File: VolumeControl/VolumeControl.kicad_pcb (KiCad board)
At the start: 2 copper layers, 5 parts, among them U2 MCP4251-xxxx-SL

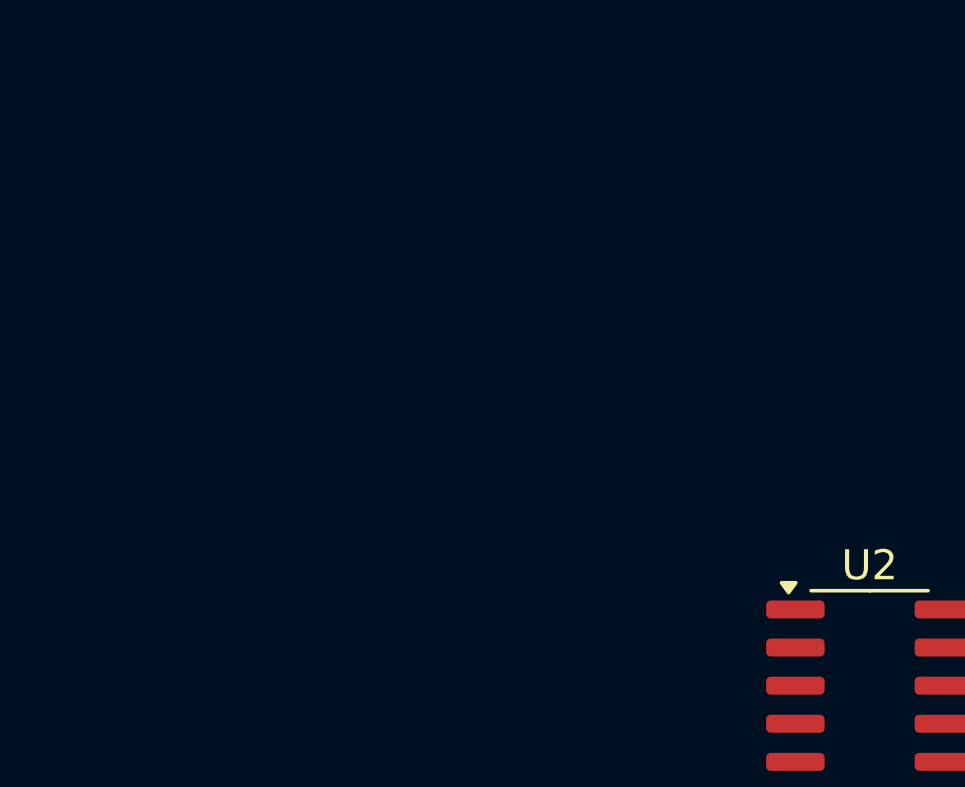
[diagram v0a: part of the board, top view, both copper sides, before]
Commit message: 6 Opamps
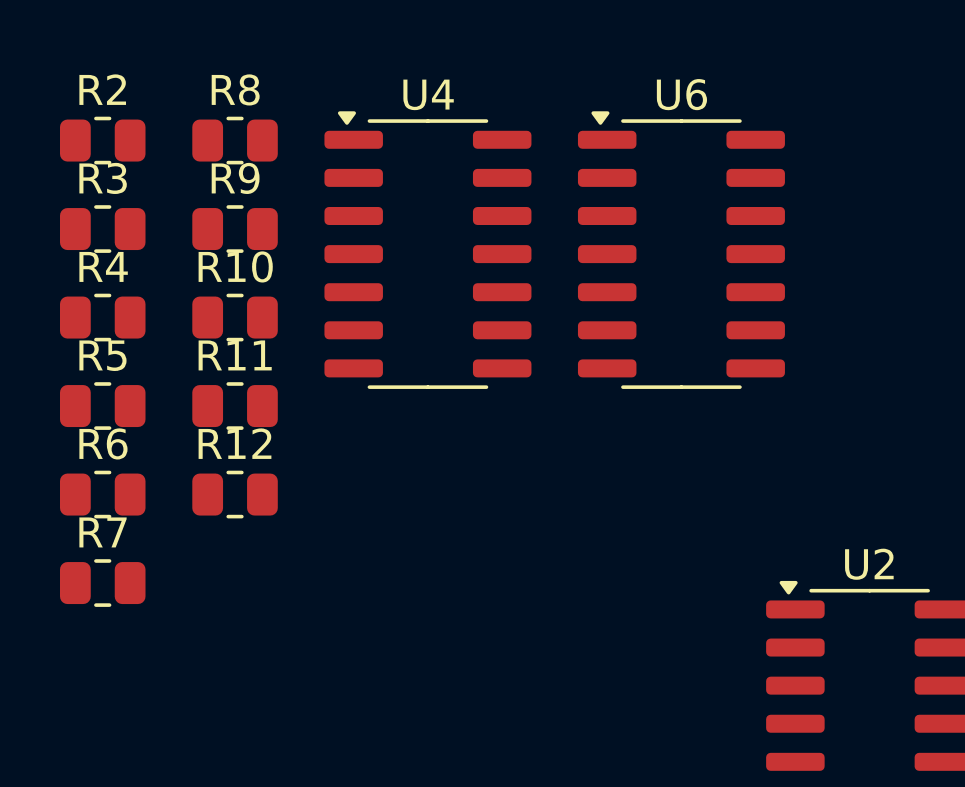
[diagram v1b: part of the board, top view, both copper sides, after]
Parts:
- added R10: 100k, Resistor_SMD:R_0805_2012Metric, F.Cu at (48.8, 44.1)
- added R11: 100k, Resistor_SMD:R_0805_2012Metric, F.Cu at (48.8, 47.1)
- added R12: 100k, Resistor_SMD:R_0805_2012Metric, F.Cu at (48.8, 50.0)
- added R2: 100k, Resistor_SMD:R_0805_2012Metric, F.Cu at (44.4, 38.2)
- added R3: 100k, Resistor_SMD:R_0805_2012Metric, F.Cu at (44.4, 41.2)
- added R4: 100k, Resistor_SMD:R_0805_2012Metric, F.Cu at (44.4, 44.1)
- added R5: 100k, Resistor_SMD:R_0805_2012Metric, F.Cu at (44.4, 47.1)
- added R6: 100k, Resistor_SMD:R_0805_2012Metric, F.Cu at (44.4, 50.0)
- added R7: 100k, Resistor_SMD:R_0805_2012Metric, F.Cu at (44.4, 53.0)
- added R8: 100k, Resistor_SMD:R_0805_2012Metric, F.Cu at (48.8, 38.2)
- added R9: 100k, Resistor_SMD:R_0805_2012Metric, F.Cu at (48.8, 41.2)
- added U4: MCP4251-xxxx-SL, Package_SO:SOIC-14_3.9x8.7mm_P1.27mm, F.Cu at (55.3, 42.0)
- added U6: MCP4251-xxxx-SL, Package_SO:SOIC-14_3.9x8.7mm_P1.27mm, F.Cu at (63.7, 42.0)
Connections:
- C1 pad 1: unconnected-(C1-Pad1) -> VCC
- C1 pad 2: unconnected-(C1-Pad2) -> GND
- D2 pad 1: unconnected-(D2-K-Pad1) -> Net-(D2-K)
- D2 pad 2: unconnected-(D2-A-Pad2) -> Net-(D2-A)
- R1 pad 1: unconnected-(R1-Pad1) -> Net-(J3-Pin_2)
- R1 pad 2: unconnected-(R1-Pad2) -> GND
- U2 pad 14: unconnected-(U2-VDD-Pad14) -> VCC
- U2 pad 4: unconnected-(U2-VSS-Pad4) -> GND
- U2 pad 7: unconnected-(U2-P1A-Pad7) -> Net-(U2-P1A)
- U2 pad 8: unconnected-(U2-P0A-Pad8) -> Net-(U2-P0A)

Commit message: circuito quase completo
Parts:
- removed D1: 1N4001, Diode_THT:D_DO-41_SOD81_P10.16mm_Horizontal
- added C10: 10u, Capacitor_SMD:C_1210_3225Metric_Pad1.33x2.70mm_HandSolder, F.Cu at (49.5, 120.7)
- added C11: 10u, Capacitor_SMD:C_1210_3225Metric_Pad1.33x2.70mm_HandSolder, F.Cu at (56.5, 137.7)
- added C12: 50p, Capacitor_SMD:C_0805_2012Metric_Pad1.18x1.45mm_HandSolder, F.Cu at (34.5, 131.7)
- added C13: 50p, Capacitor_SMD:C_0805_2012Metric_Pad1.18x1.45mm_HandSolder, F.Cu at (41.5, 141.7)
- added C14: 10u, Capacitor_SMD:C_1210_3225Metric_Pad1.33x2.70mm_HandSolder, F.Cu at (35.5, 127.7)
- added C15: 10u, Capacitor_SMD:C_1210_3225Metric_Pad1.33x2.70mm_HandSolder, F.Cu at (42.5, 137.7)
- added C16: 10u, Capacitor_SMD:C_1210_3225Metric_Pad1.33x2.70mm_HandSolder, F.Cu at (42.5, 127.7)
- added C17: 10u, Capacitor_SMD:C_1210_3225Metric_Pad1.33x2.70mm_HandSolder, F.Cu at (42.5, 122.7)
- added C18: 50p, Capacitor_SMD:C_0805_2012Metric_Pad1.18x1.45mm_HandSolder, F.Cu at (46.5, 141.7)
- added C19: 50p, Capacitor_SMD:C_0805_2012Metric_Pad1.18x1.45mm_HandSolder, F.Cu at (50.5, 101.7)
- added C2: 100uF, Capacitor_SMD:CP_Elec_5x3.9, F.Cu at (52.5, 112.7)
- added C20: 10u, Capacitor_SMD:C_1210_3225Metric_Pad1.33x2.70mm_HandSolder, F.Cu at (49.5, 137.7)
- added C21: 10u, Capacitor_SMD:C_1210_3225Metric_Pad1.33x2.70mm_HandSolder, F.Cu at (56.5, 101.7)
- added C22: 50p, Capacitor_SMD:C_0805_2012Metric_Pad1.18x1.45mm_HandSolder, F.Cu at (47.5, 107.7)
- added C23: 50p, Capacitor_SMD:C_0805_2012Metric_Pad1.18x1.45mm_HandSolder, F.Cu at (42.5, 109.7)
- added C24: 100nF, Capacitor_SMD:C_0805_2012Metric, F.Cu at (43.5, 118.7)
- added C25: 100nF, Capacitor_SMD:C_0805_2012Metric, F.Cu at (45.5, 115.7)
- added C26: 100nF, Capacitor_SMD:C_0805_2012Metric, F.Cu at (40.5, 115.7)
- added C27: 100nF, Capacitor_SMD:C_0805_2012Metric, F.Cu at (40.5, 112.7)
- added C28: 100nF, Capacitor_SMD:C_0805_2012Metric, F.Cu at (63.5, 88.7)
- added C29: 100uF, Capacitor_SMD:CP_Elec_5x3.9, F.Cu at (70.5, 94.7)
- added C3: 100uF, Capacitor_SMD:CP_Elec_5x3.9, F.Cu at (70.5, 101.7)
- added C4: 10u, Capacitor_SMD:C_1210_3225Metric_Pad1.33x2.70mm_HandSolder, F.Cu at (56.5, 96.7)
- added C5: 50p, Capacitor_SMD:C_0805_2012Metric_Pad1.18x1.45mm_HandSolder, F.Cu at (50.5, 97.7)
- added C6: 50p, Capacitor_SMD:C_0805_2012Metric_Pad1.18x1.45mm_HandSolder, F.Cu at (42.5, 106.7)
- added C7: 10u, Capacitor_SMD:C_1210_3225Metric_Pad1.33x2.70mm_HandSolder, F.Cu at (53.5, 106.7)
- added C8: 10u, Capacitor_SMD:C_1210_3225Metric_Pad1.33x2.70mm_HandSolder, F.Cu at (80.5, 95.7)
- added C9: 10u, Capacitor_SMD:C_1210_3225Metric_Pad1.33x2.70mm_HandSolder, F.Cu at (96.5, 98.5)
- added J1: Barrel_Jack, Connector_BarrelJack:BarrelJack_CUI_PJ-063AH_Horizontal, F.Cu at (115.5, 77.0)
- added J10: Conn_01x03, Connector_PinHeader_1.00mm:PinHeader_1x03_P1.00mm_Vertical, F.Cu at (41.5, 131.7)
- added J11: Conn_01x03, Connector_PinHeader_1.00mm:PinHeader_1x03_P1.00mm_Vertical, F.Cu at (38.5, 131.7)
- added J12: Conn_01x03, Connector_PinHeader_1.00mm:PinHeader_1x03_P1.00mm_Vertical, F.Cu at (53.5, 131.7)
- added J13: Conn_01x03, Connector_PinHeader_1.00mm:PinHeader_1x03_P1.00mm_Vertical, F.Cu at (61.5, 102.7)
- added J2: Conn_01x03, Connector_PinHeader_1.00mm:PinHeader_1x03_P1.00mm_Vertical, F.Cu at (64.5, 102.7)
- added J3: Conn_01x03, Connector_PinHeader_1.00mm:PinHeader_1x03_P1.00mm_Vertical, F.Cu at (61.5, 97.7)
- added J4: Conn_01x03, Connector_PinHeader_1.00mm:PinHeader_1x03_P1.00mm_Vertical, F.Cu at (50.5, 131.7)
- added J5: Conn_01x03, Connector_PinHeader_1.00mm:PinHeader_1x03_P1.00mm_Vertical, F.Cu at (64.5, 97.7)
- added J6: Conn_01x03, Connector_PinHeader_1.00mm:PinHeader_1x03_P1.00mm_Vertical, F.Cu at (47.5, 126.7)
- added J7: Conn_01x03, Connector_PinHeader_1.00mm:PinHeader_1x03_P1.00mm_Vertical, F.Cu at (56.5, 131.7)
- added J8: Conn_01x03, Connector_PinHeader_1.00mm:PinHeader_1x03_P1.00mm_Vertical, F.Cu at (44.5, 131.7)
- added J9: Conn_01x03, Connector_PinHeader_1.00mm:PinHeader_1x03_P1.00mm_Vertical, F.Cu at (47.5, 131.7)
- added R13: 100k, Resistor_SMD:R_0805_2012Metric, F.Cu at (47.5, 104.7)
- added R14: 100k, Resistor_SMD:R_0805_2012Metric, F.Cu at (42.5, 103.7)
- added R15: 100k, Resistor_SMD:R_0805_2012Metric, F.Cu at (58.5, 92.7)
- added U1: OPA1612AxD, Package_SO:SOIC-8-1EP_3.9x4.9mm_P1.27mm_EP2.29x3mm, F.Cu at (79.5, 101.7)
- added U10: LM1117MP-5.0, Package_TO_SOT_SMD:SOT-223-3_TabPin2, F.Cu at (70.5, 109.7)
- added U3: L7812, Package_TO_SOT_SMD:TO-252-3_TabPin2, F.Cu at (131.6, 75.7)
- added U5: OPA1612AxD, Package_SO:SOIC-8-1EP_3.9x4.9mm_P1.27mm_EP2.29x3mm, F.Cu at (55.5, 126.7)
- added U7: OPA1612AxD, Package_SO:SOIC-8-1EP_3.9x4.9mm_P1.27mm_EP2.29x3mm, F.Cu at (57.5, 119.7)
- added U8: OPA1612AxD, Package_SO:SOIC-8-1EP_3.9x4.9mm_P1.27mm_EP2.29x3mm, F.Cu at (61.5, 110.7)
- added U9: WEMOS_D1_mini, RF_Module:WEMOS_D1_mini_light, F.Cu at (63.5, 133.7)
- C1: footprint Capacitor_SMD:C_0805_2012Metric -> Capacitor_SMD:C_0805_2012Metric_Pad1.18x1.45mm_HandSolder
- moved C1 566.3 mm to (45.5, 112.7)
- moved R1 549.2 mm to (63.5, 94.7)
- moved D2 486.1 mm to (122.0, 76.5), turned to 180 degrees
- moved R2 106.6 mm to (49.5, 144.7)
- moved R8 106.6 mm to (44.5, 144.7)
- moved R11 97.8 mm to (54.5, 144.7)
- moved R9 94.8 mm to (33.5, 134.7)
- moved R6 92.3 mm to (55.5, 141.7)
- moved R10 89.7 mm to (29.5, 131.7)
- moved U4 80.3 mm to (75.5, 119.7)
- moved U6 77.7 mm to (66.5, 119.7)
- moved R5 74.0 mm to (36.5, 120.7)
- moved R7 71.2 mm to (36.5, 123.7)
- moved U2 63.7 mm to (84.5, 119.7)
- moved R3 60.9 mm to (78.5, 91.7)
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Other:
- board outline added: 116.5 x 76.5 mm
- board text added: "0.0000 mm / 0.0000 mm"
- board text added: "0.3000 mm"
- board text added: "1.6000 mm"
- board text added: "2"
- board text added: "81.5808 mm x 89.8315 mm"
- board text added: "BOARD CHARACTERISTICS"
- board text added: "Board Thickness:"
- board text added: "Board overall dimensions:"
- board text added: "Castellated pads:"
- board text added: "Copper Finish:"
- board text added: "Copper Layer Count:"
- board text added: "Edge card connectors:"
- board text added: "Impedance Control:"
- board text added: "Min hole diameter:"
- board text added: "Min track/spacing:"
- board text added: "No"
- board text added: "None"
- board text added: "Plated Board Edge:"

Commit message: layout upates
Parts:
- added D1: LED, LED_SMD:LED_1210_3225Metric, F.Cu at (150.5, 78.6)
- added R16: 560R, Resistor_SMD:R_0805_2012Metric, F.Cu at (150.5, 74.0)
- moved C28 113.5 mm to (176.5, 78.5), turned to 90 degrees
- moved J4 112.5 mm to (160.5, 108.0)
- moved R2 110.7 mm to (153.9, 108.0)
- moved C6 102.8 mm to (145.0, 114.5), turned to 90 degrees
- moved C29 102.7 mm to (171.5, 76.2), turned to 90 degrees
- moved J3 99.0 mm to (160.5, 98.0)
- moved C2 99.0 mm to (144.0, 75.0), turned to 90 degrees
- moved C1 96.4 mm to (138.0, 85.5), turned to 180 degrees
- moved U10 96.2 mm to (161.0, 77.0)
- moved C5 95.2 mm to (145.5, 104.0), turned to 90 degrees
- moved C7 93.5 mm to (146.9, 109.5)
- moved R1 90.6 mm to (154.0, 98.5)
- moved C4 90.0 mm to (146.4, 98.5)
- moved C3 64.8 mm to (129.5, 75.0), turned to 90 degrees
- moved R4 59.0 mm to (119.6, 110.0)
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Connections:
- U2 pad 14: VCC -> V5V
- U4 pad 14: VCC -> V5V
- U6 pad 14: VCC -> V5V
- U9 pad 14: unconnected-(U9-SCL/D1-Pad14) -> SCL
- U9 pad 4: unconnected-(U9-SCK/D5-Pad4) -> SCK
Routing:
- net GND: track 0.00 -> 91.6 mm
- net VCC: track 0.00 -> 23.7 mm
- net Net-(D2-K): track 0.00 -> 13.9 mm
- net V5V: track 0.00 -> 13.3 mm
- net Net-(D2-A): track 0.00 -> 4.71 mm
- net Net-(D1-K): track 0.00 -> 2.29 mm
- added copper zone on F.Cu, net GND
- added copper zone on F.Cu, net V5V
- added copper zone on F.Cu, net VCC

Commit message: improvements on PCB design - PCB placement finished -missing controller
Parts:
- added FB1: FerriteBead_Small, Resistor_SMD:R_1206_3216Metric_Pad1.30x1.75mm_HandSolder, F.Cu at (112.0, 78.0)
- added R17: 10R, Resistor_SMD:R_0805_2012Metric, F.Cu at (115.5, 78.1)
- U1, U5, U7, U8: footprint Package_SO:SOIC-8-1EP_3.9x4.9mm_P1.27mm_EP2.29x3mm -> Package_SO:SOIC-8_3.9x4.9mm_P1.27mm
- moved R7 142.4 mm to (178.5, 113.6), turned to 90 degrees
- moved C22 139.3 mm to (182.5, 73.6), turned to 180 degrees
- moved J8 138.6 mm to (182.0, 114.1)
- moved C12 137.6 mm to (170.6, 111.1), turned to 180 degrees
- moved C14 136.1 mm to (171.0, 114.1)
- moved R8 135.2 mm to (178.5, 126.6), turned to 90 degrees
- moved J9 134.6 mm to (182.0, 126.6)
- moved R13 134.4 mm to (178.5, 74.6), turned to 90 degrees
- moved R12 133.2 mm to (178.5, 147.6), turned to 90 degrees
- moved C23 133.2 mm to (173.5, 85.6), turned to 180 degrees
- moved R14 132.8 mm to (172.1, 74.6)
- moved C27 132.0 mm to (168.0, 78.6), turned to -90 degrees
- moved C13 130.7 mm to (171.0, 124.1), turned to 180 degrees
- moved C15 129.0 mm to (171.1, 127.6)
- moved J12 128.7 mm to (182.0, 138.1)
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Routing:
- net GND: track 91.6 -> 203.7 mm, vias 0 -> 3
- net Earth: track 0.00 -> 44.5 mm
- net Net-(U1B--): track 0.00 -> 39.7 mm
- net Net-(U1A-+): track 0.00 -> 29.5 mm, vias 0 -> 2
- net Net-(U1A--): track 0.00 -> 21.7 mm
- net VCC: track 23.7 -> 45.3 mm
- net Net-(U2-P0A): track 0.00 -> 17.5 mm
- net Net-(U2-P1A): track 0.00 -> 17.1 mm
- net Net-(R15-Pad1): track 0.00 -> 12.1 mm
- net Net-(U1B-+): track 0.00 -> 12.0 mm
- net Net-(U8A-+): track 0.00 -> 10.5 mm
- net Net-(J3-Pin_2): track 0.00 -> 9.71 mm
- net Net-(J4-Pin_2): track 0.00 -> 9.57 mm
- net Net-(J2-Pin_2): track 0.00 -> 9.19 mm
- net Net-(J5-Pin_2): track 0.00 -> 9.15 mm
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- added copper zone on F.Cu, net Earth
- added copper zone on B.Cu, net GND
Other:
- board size 116.5 x 76.5 mm -> 76.5 x 94.5 mm

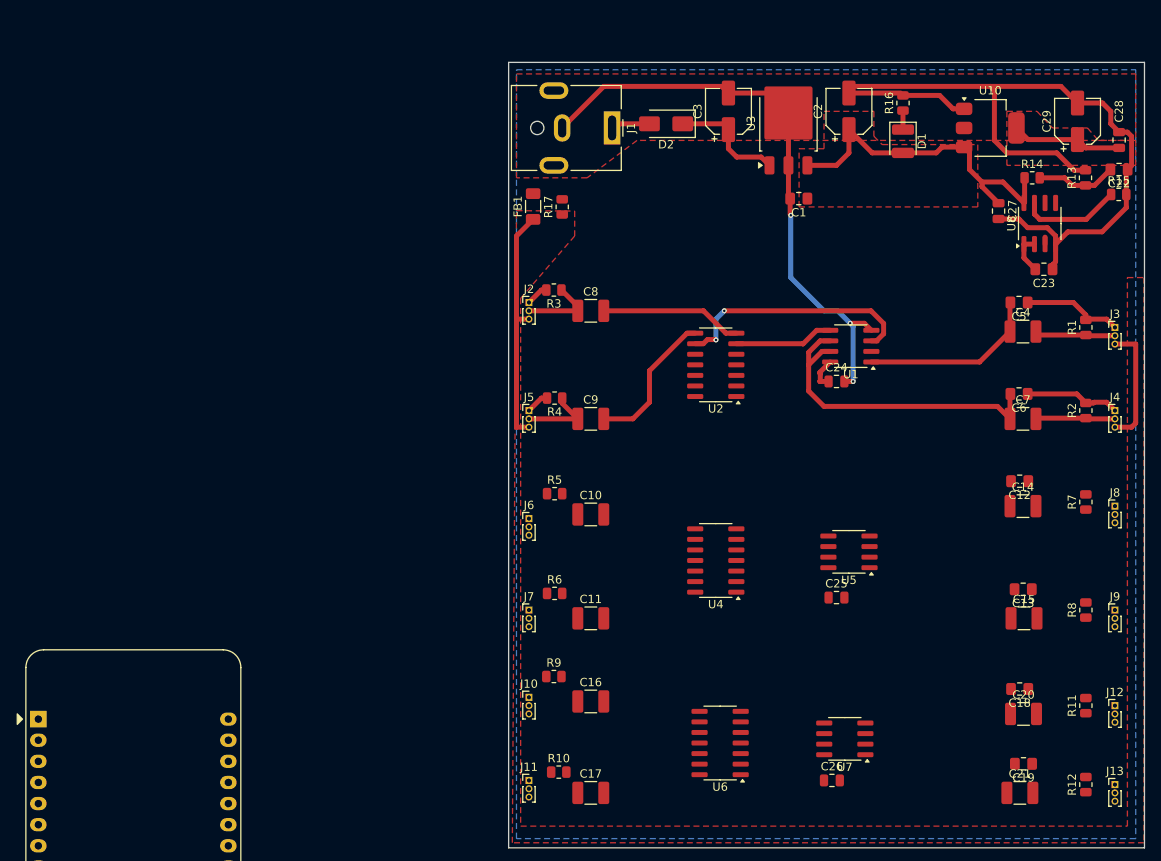
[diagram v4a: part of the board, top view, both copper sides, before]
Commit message: simulation update, schematic update for only one input
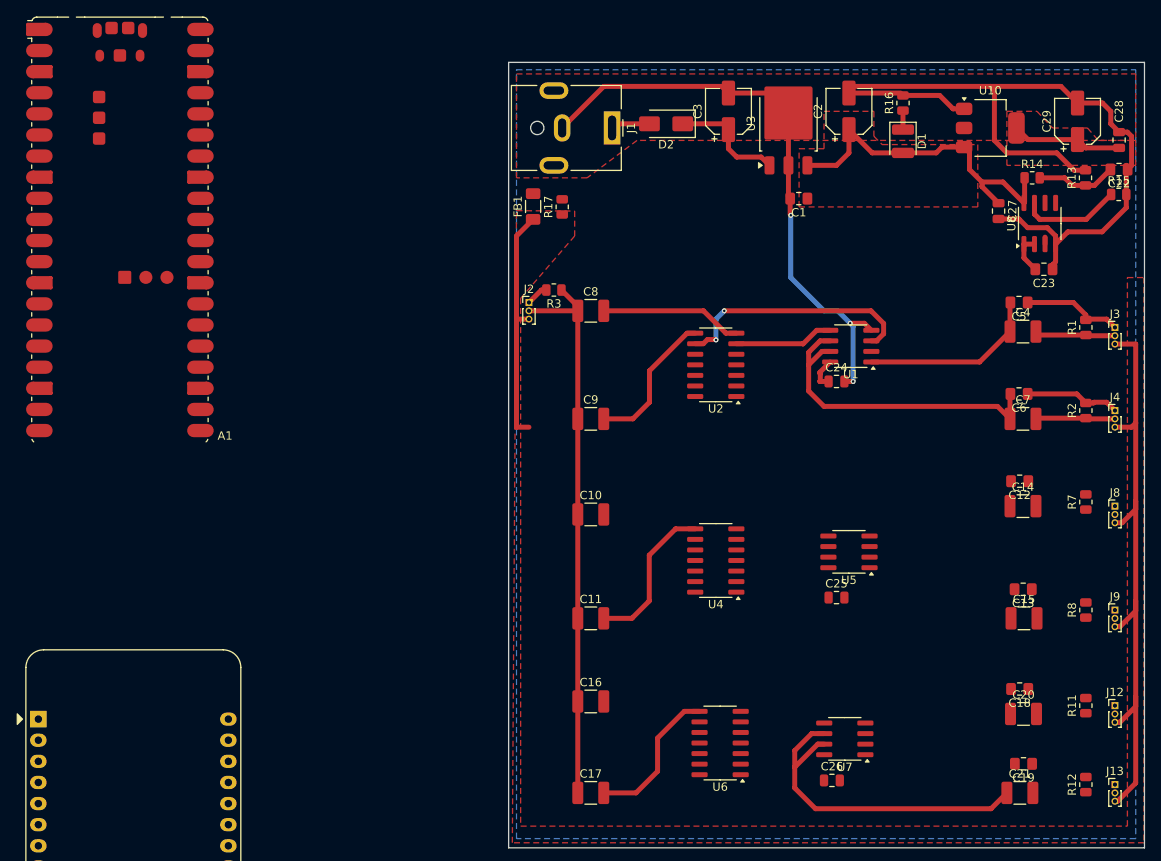
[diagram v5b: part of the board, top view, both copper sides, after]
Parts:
- removed J10, J11, J5, J6, J7: Conn_01x03, Connector_PinHeader_1.00mm:PinHeader_1x03_P1.00mm_Vertical
- removed R10, R4, R5, R6, R9: 100k, Resistor_SMD:R_0805_2012Metric
- added A1: RaspberryPi_Pico_W, Module:RaspberryPi_Pico_W_SMD, F.Cu at (62.3, 80.9)
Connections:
- C10 pad 1: Net-(J6-Pin_2) -> Net-(J2-Pin_2)
- C10 pad 2: Net-(U4-P1A) -> Net-(U2-P1A)
- C11 pad 1: Net-(J7-Pin_2) -> Net-(J2-Pin_2)
- C16 pad 1: Net-(J10-Pin_2) -> Net-(J2-Pin_2)
- C17 pad 1: Net-(J11-Pin_2) -> Net-(J2-Pin_2)
- C9 pad 1: Net-(J5-Pin_2) -> Net-(J2-Pin_2)
- U2 pad 13: unconnected-(U2-SDO-Pad13) -> Net-(U2-P1A)
- U4 pad 7: Net-(U4-P1A) -> Net-(U2-P1A)
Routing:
- net Earth: track 44.5 -> 104.4 mm
- net Net-(J2-Pin_2): track 9.19 -> 67.2 mm
- net Net-(U7B--): track 0.00 -> 40.9 mm
- net Net-(U4-P0A): track 0.00 -> 18.7 mm
- net Net-(U6-P0A): track 0.00 -> 17.9 mm
- net Net-(J5-Pin_2): track 9.15 -> 0.00 mm
- net GND: track 203.7 -> 200.9 mm

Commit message: PPT first draft
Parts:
- removed A1: RaspberryPi_Pico_W, Module:RaspberryPi_Pico_W_SMD
- removed U9: WEMOS_D1_mini, RF_Module:WEMOS_D1_mini_light
- added D3: LED, LED_SMD:LED_1210_3225Metric, F.Cu at (312.4, 117.3)
- added D4: LED, LED_SMD:LED_1210_3225Metric, F.Cu at (312.4, 121.6)
- added D5: LED, LED_SMD:LED_1210_3225Metric, F.Cu at (312.4, 125.8)
- added D6: LED, LED_SMD:LED_1210_3225Metric, F.Cu at (312.4, 130.1)
- added D7: LED, LED_SMD:LED_1210_3225Metric, F.Cu at (312.4, 134.4)
- added D8: LED, LED_SMD:LED_1210_3225Metric, F.Cu at (312.4, 138.7)
- added R10: 100R, Resistor_SMD:R_0805_2012Metric, F.Cu at (330.2, 119.5)
- added R18: 100R, Resistor_SMD:R_0805_2012Metric, F.Cu at (330.2, 122.5)
- added R19: 10K, Resistor_SMD:R_0805_2012Metric, F.Cu at (334.6, 116.6)
- added R20: 10K, Resistor_SMD:R_0805_2012Metric, F.Cu at (334.6, 119.5)
- added R21: 10K, Resistor_SMD:R_0805_2012Metric, F.Cu at (334.6, 122.5)
- added R4: 100R, Resistor_SMD:R_0805_2012Metric, F.Cu at (325.8, 116.6)
- added R5: 100R, Resistor_SMD:R_0805_2012Metric, F.Cu at (325.8, 119.5)
- added R6: 100R, Resistor_SMD:R_0805_2012Metric, F.Cu at (325.8, 122.5)
- added R9: 100R, Resistor_SMD:R_0805_2012Metric, F.Cu at (330.2, 116.6)
- added SW1: Select, Button_Switch_SMD:SW_SPST_PTS647_Sx50, F.Cu at (319.4, 118.3)
- added SW2: Up, Button_Switch_SMD:SW_SPST_PTS647_Sx50, F.Cu at (319.4, 124.8)
- added SW3: Down, Button_Switch_SMD:SW_SPST_PTS647_Sx50, F.Cu at (319.4, 131.2)
- added U12: ESP32-S3-DevKitC, Espressif:ESP32-S3-DevKitC, F.Cu at (189.7, 148.0)
- moved C23 81.2 mm to (246.0, 49.1)
- moved R13 81.2 mm to (251.0, 38.1)
- moved R14 81.2 mm to (244.5, 38.1)
- moved R15 81.2 mm to (255.0, 40.1)
- moved U2 81.2 mm to (206.5, 60.6)
- moved U4 81.2 mm to (206.5, 84.1)
- moved U8 81.2 mm to (245.5, 43.6)
- moved C12 81.2 mm to (243.0, 74.6)
- moved C18 81.2 mm to (243.0, 99.6)
- moved C26 81.2 mm to (220.5, 110.6)
- moved C1 81.2 mm to (216.5, 40.6)
- moved C10 81.2 mm to (191.4, 78.6)
- moved C11 81.2 mm to (191.4, 91.1)
- moved C13 81.2 mm to (243.5, 87.6)
- moved C14 81.2 mm to (243.4, 77.6)
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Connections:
- C10 pad 2: Net-(U2-P1A) -> Net-(U4-P1A)
- U2 pad 1: unconnected-(U2-~{CS}-Pad1) -> CS0
- U2 pad 13: Net-(U2-P1A) -> MISO
- U2 pad 2: unconnected-(U2-SCK-Pad2) -> SCK
- U2 pad 3: unconnected-(U2-SDI-Pad3) -> MOSI
- U4 pad 1: unconnected-(U4-~{CS}-Pad1) -> CS1
- U4 pad 13: unconnected-(U4-SDO-Pad13) -> MISO
- U4 pad 2: unconnected-(U4-SCK-Pad2) -> SCK
- U4 pad 3: unconnected-(U4-SDI-Pad3) -> MOSI
- U4 pad 7: Net-(U2-P1A) -> Net-(U4-P1A)
- U6 pad 1: unconnected-(U6-~{CS}-Pad1) -> CS2
- U6 pad 13: unconnected-(U6-SDO-Pad13) -> MISO
- U6 pad 2: unconnected-(U6-SCK-Pad2) -> SCK
- U6 pad 3: unconnected-(U6-SDI-Pad3) -> MOSI
